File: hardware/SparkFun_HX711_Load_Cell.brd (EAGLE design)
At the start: 30.5 x 22.9 mm, 30 parts, among them Q1 MMBT4403, U1 HX711, U7 OSHW-LOGOS

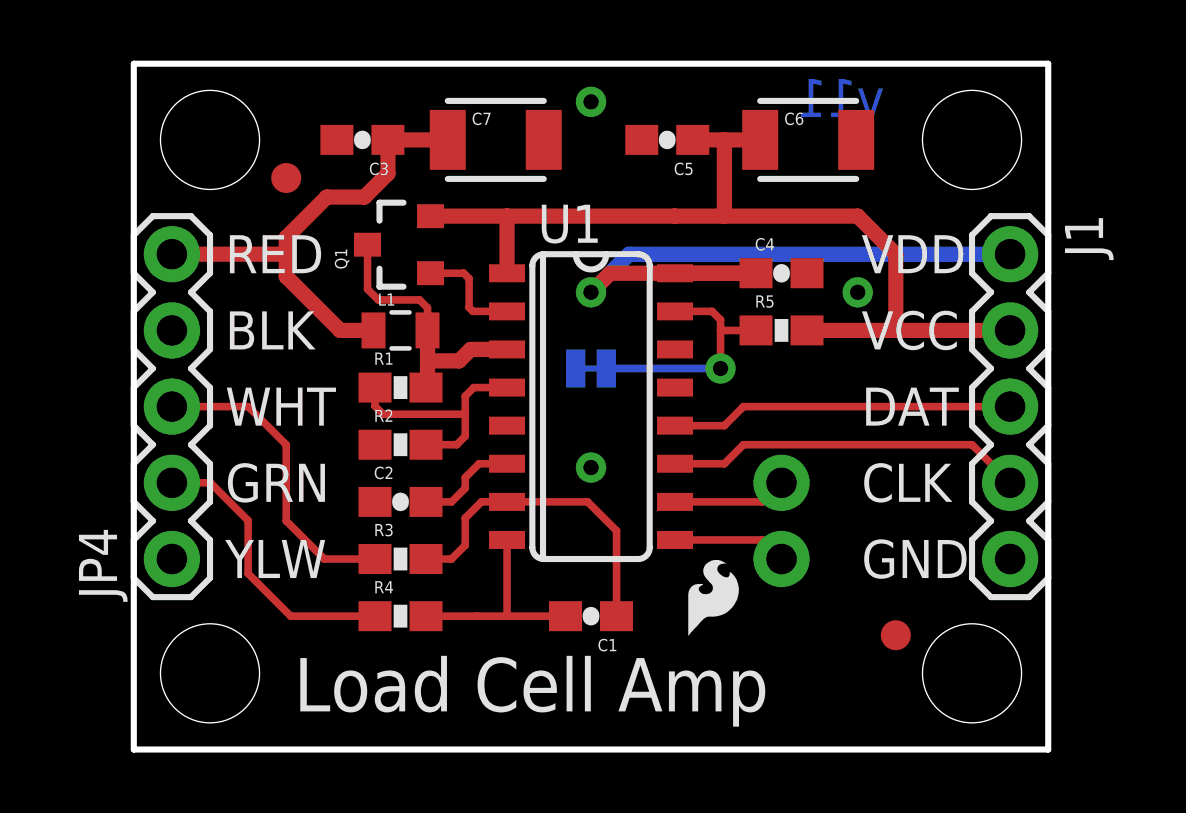
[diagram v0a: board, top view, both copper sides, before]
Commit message: V11 Update
Removed spaces from file names
Fixed silk causing CAM errors
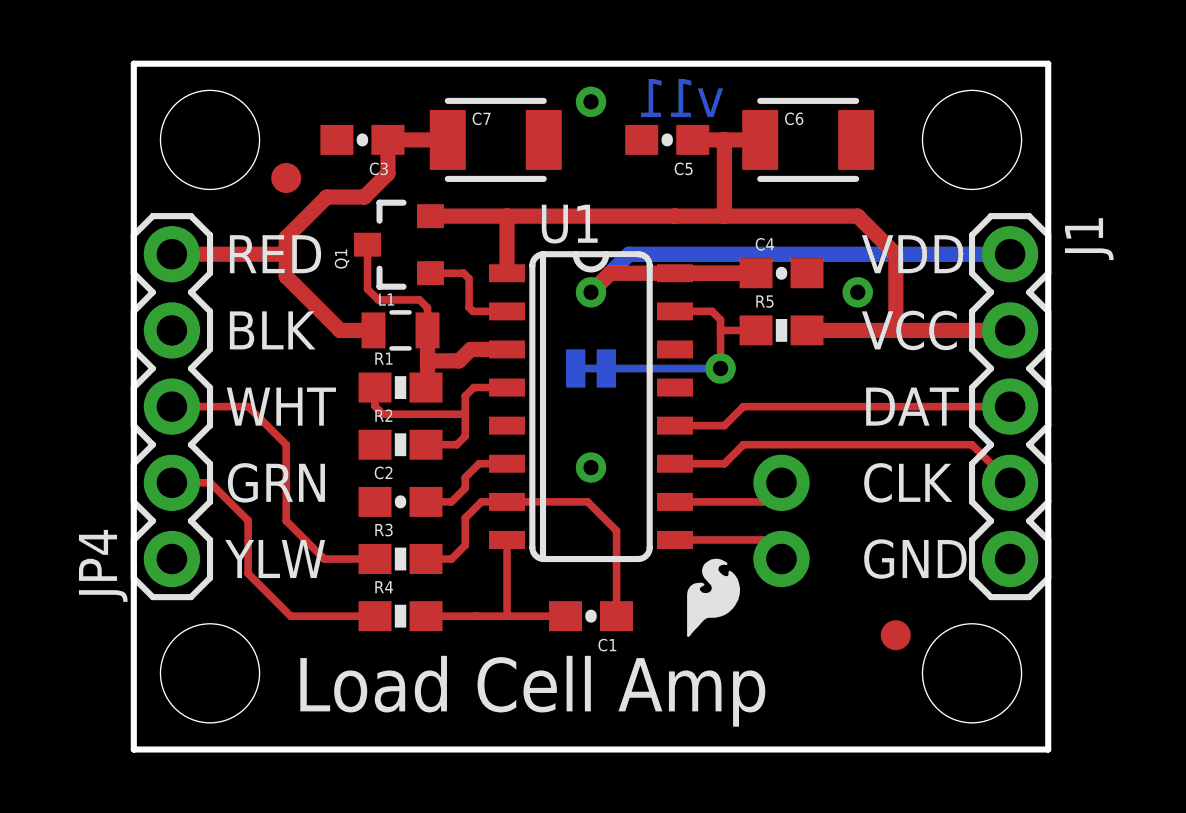
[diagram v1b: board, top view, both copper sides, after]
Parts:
- FRAME1: value (none) -> FRAME-LETTER
- R1: value 20K -> 20k
- moved U$1 3.81 mm to (6.99, -22.9)
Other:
- board text added: "N. Seidle"
- board text added: "v11"
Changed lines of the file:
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@@
 <text x="24.257" y="15.875" size="1.27" layer="21" font="vector" ratio="15">VDD</text>
 <text x="25.4" y="-22.86" size="1.778" layer="51" font="vector" ratio="15">Alex Wende</text>
+<text x="25.4" y="-19.05" size="1.778" layer="51" font="vector" ratio="15">N. Seidle</text>
+<text x="19.685" y="21.082" size="1.27" layer="16" font="vector" ratio="20" rot="MR0">v11</text>
 </plain>
 <attributes>
@@
 <attribute name="PROD_ID" value="RES-10646" x="8.89" y="10.16" size="1.778" layer="27" font="vector" ratio="15" display="off"/>
 </element>
-<element name="R1" library="SparkFun-Resistors" package="0603-RES" value="20K" x="8.89" y="12.065">
+<element name="R1" library="SparkFun-Resistors" package="0603-RES" value="20k" x="8.89" y="12.065">
 <attribute name="PROD_ID" value="RES-09383" x="8.89" y="12.065" size="1.778" layer="27" font="vector" ratio="15" display="off"/>
 </element>
@@
 <attribute name="PROD_ID" value="CAP-08604" x="7.62" y="20.32" size="1.778" layer="27" font="vector" ratio="15" rot="R180" display="off"/>
 </element>
-<element name="FRAME1" library="SparkFun-Aesthetics" package="CREATIVE_COMMONS" value="" x="-5.08" y="-19.05" smashed="yes">
-<attribute name="VERSION" value="v11" x="22.098" y="22.352" size="1.27" layer="16" font="vector" ratio="20" rot="MR180"/>
-<attribute name="DESIGNER" value="N. Seidle" x="25.4" y="-19.05" size="1.778" layer="51"/>
-</element>
+<element name="FRAME1" library="SparkFun-Aesthetics" package="CREATIVE_COMMONS" value="FRAME-LETTER" x="-5.08" y="-19.05" smashed="yes"/>
 <element name="J1" library="SparkFun-Connectors" package="1X05" value="" x="29.21" y="16.51" rot="R270"/>
 <element name="L1" library="SparkFun-Passives" package="0805" value="3.3uH" x="8.89" y="13.97">
@@
 <attribute name="PROD_ID" value="CAP-08604" x="21.59" y="15.875" size="1.778" layer="27" font="vector" ratio="15" display="off"/>
 </element>
-<element name="U$1" library="SparkFun-Aesthetics" package="REVISION" value="REVISION" x="3.175" y="-22.86"/>
+<element name="U$1" library="SparkFun-Aesthetics" package="REVISION" value="REVISION" x="6.985" y="-22.86"/>
 </elements>
 <signals>
